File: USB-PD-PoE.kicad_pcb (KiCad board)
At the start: 4 copper layers, 39.6 x 87.4 mm, 129 parts, among them J1 8P8C_Shielded, J2 8P8C_Shielded, J3 TagConnect_TC2030_SWD, J4 USB_C_Receptacle_USB2.0, Q1 FDC2512, Q2 2N7002, Q3 2N7002, Q4 2N7002, Q5 APM4953KC, T1 HR051142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

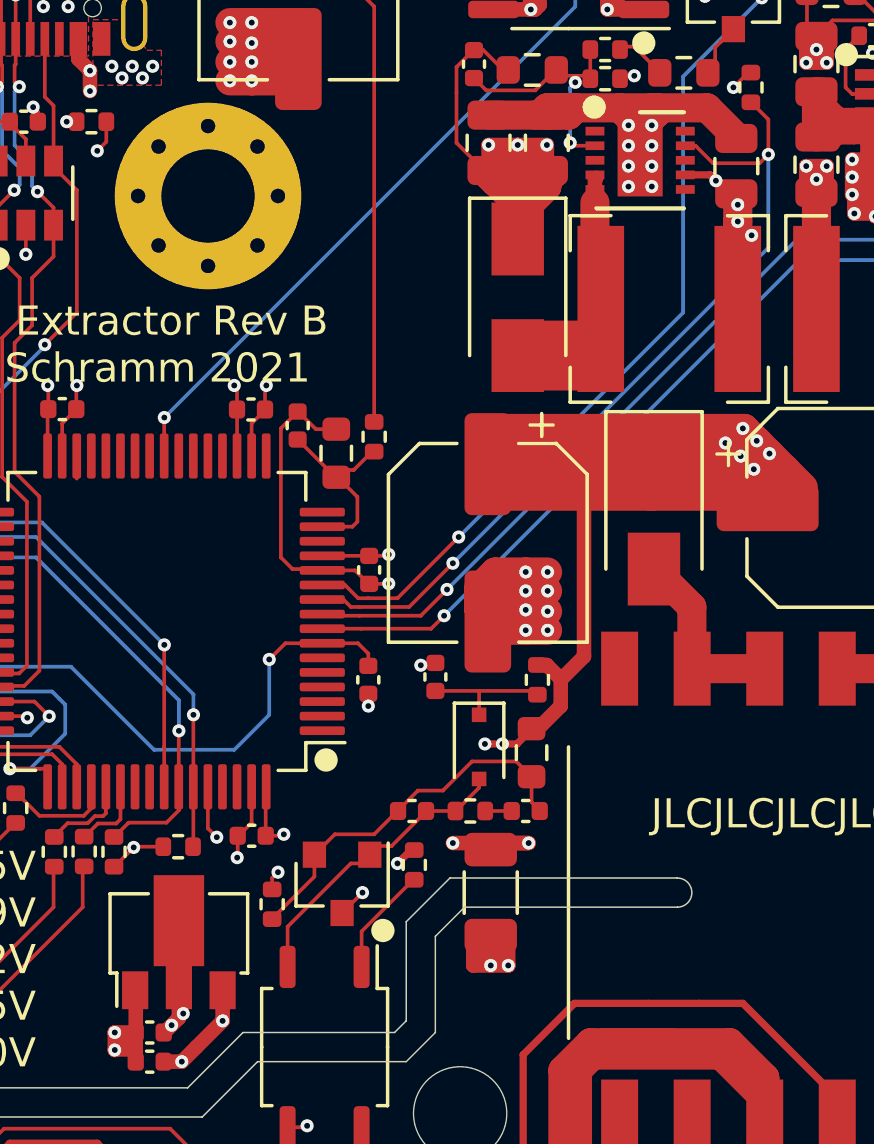
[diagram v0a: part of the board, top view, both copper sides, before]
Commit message: Fix reversed CJ431 pinout
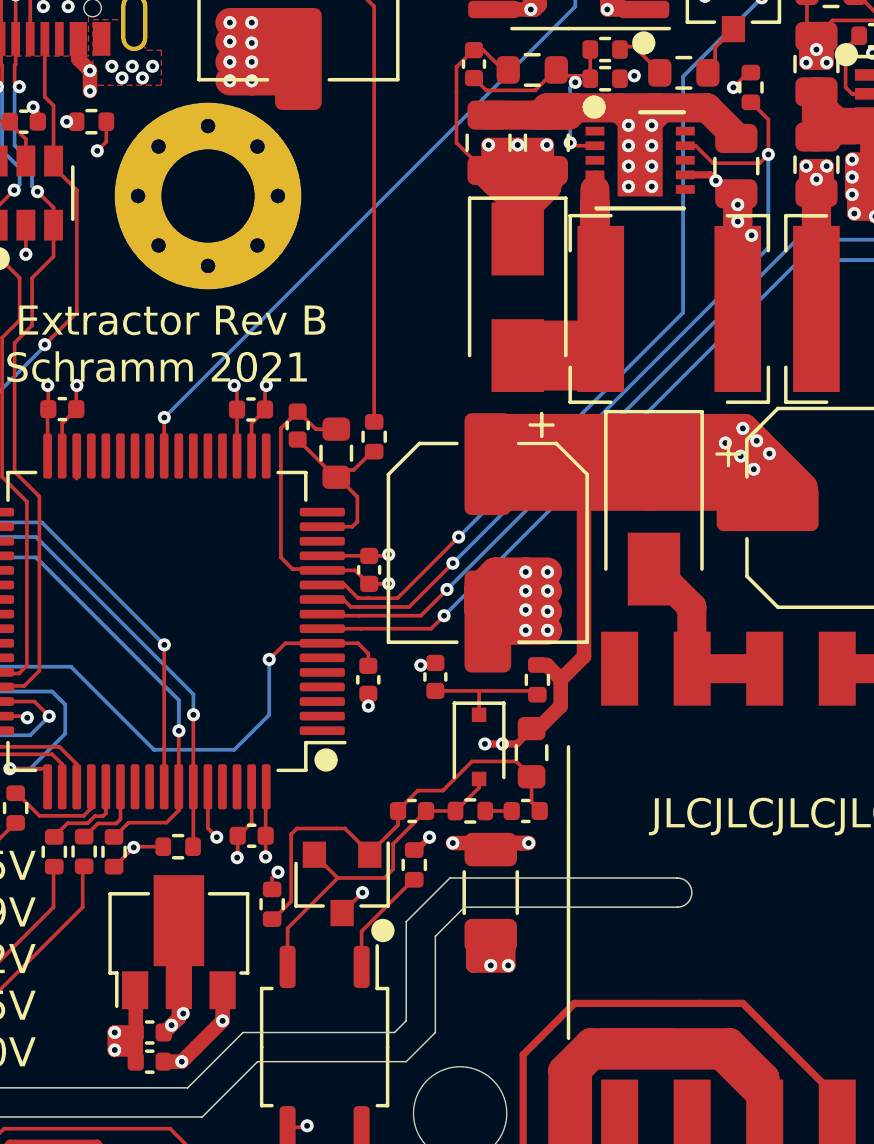
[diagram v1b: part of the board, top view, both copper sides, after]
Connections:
- U4 pad 1: Net-(C12-Pad2) -> Net-(C12-Pad1)
- U4 pad 2: Net-(C12-Pad1) -> Net-(C12-Pad2)
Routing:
- net Net-(D8-Pad2): track 19.7 -> 23.9 mm
- net Net-(C12-Pad1): track 13.1 -> 15.3 mm
- net Net-(C12-Pad2): track 9.97 -> 11.8 mm

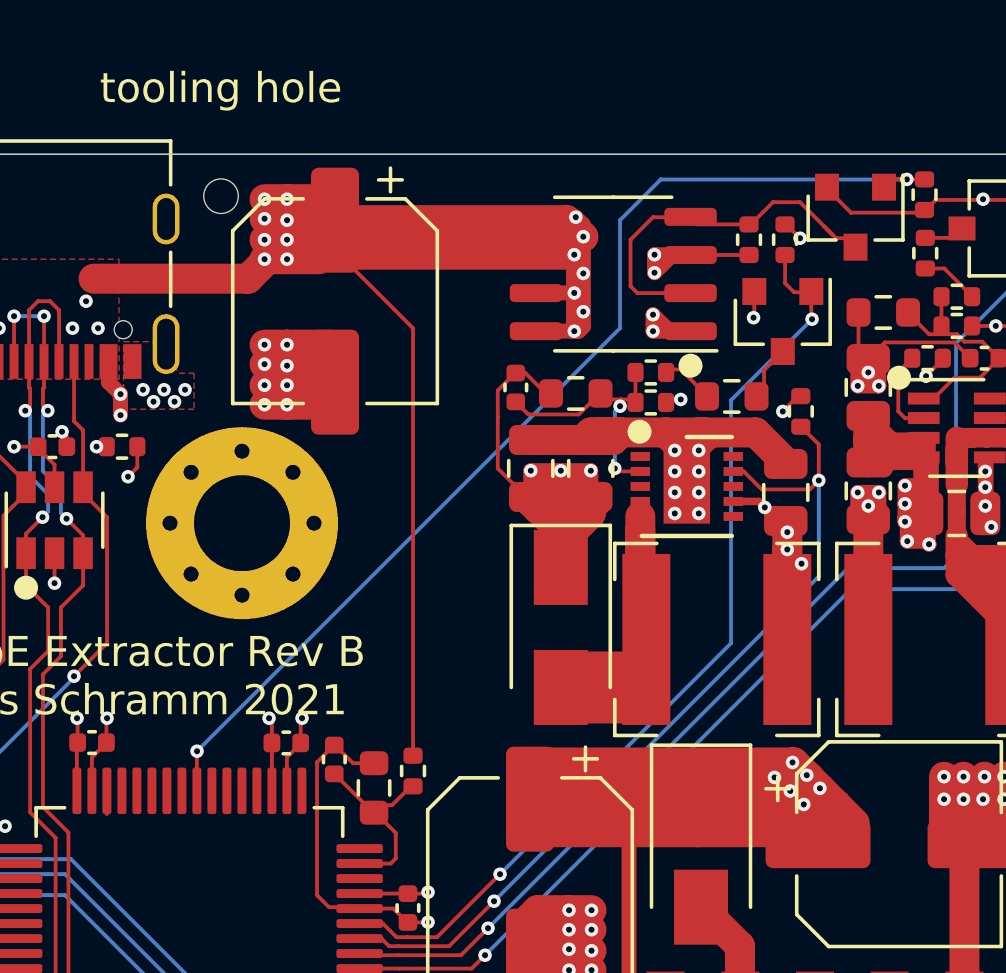
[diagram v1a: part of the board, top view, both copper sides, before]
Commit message: Add buck converter power gating
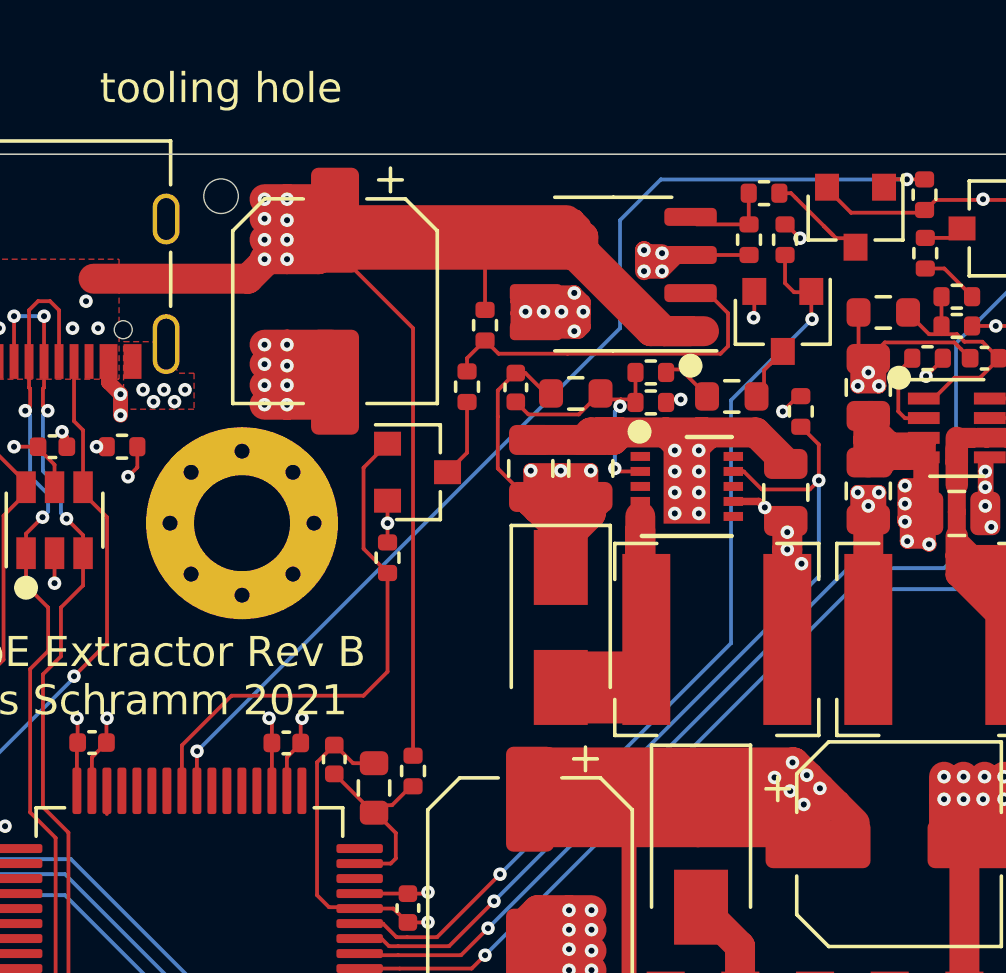
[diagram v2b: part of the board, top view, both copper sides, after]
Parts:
- added Q6: 2N7002, Package_TO_SOT_SMD:SOT-23, F.Cu at (118.5, 76.6)
- added R50: 100kR, Resistor_SMD:R_0402_1005Metric, F.Cu at (117.5, 79.5)
- added R51: 100kR, Resistor_SMD:R_0402_1005Metric, F.Cu at (120.7, 71.7)
- added R52: 15kR, Resistor_SMD:R_0402_1005Metric, F.Cu at (120.1, 73.8)
- added R53: 10kR, Resistor_SMD:R_0402_1005Metric, F.Cu at (130.0, 67.3)
- C10, C11: value 22uF EL -> 220uF EL
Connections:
- C29 pad 1: VBUS -> /BUCK_OUT
- C31 pad 1: VBUS -> /BUCK_OUT
- C39 pad 1: VBUS -> /BUCK_OUT
- L3 pad 2: VBUS -> /BUCK_OUT
- Q5 pad 1: /BOOST_OUT -> VBUS
- Q5 pad 2: Net-(Q4-Pad3) -> Net-(Q5-Pad2)
- Q5 pad 4: Net-(Q4-Pad3) -> Net-(Q5-Pad4)
- Q5 pad 7: VBUS -> /BUCK_OUT
- Q5 pad 8: VBUS -> /BUCK_OUT
- R31 pad 1: VBUS -> /BUCK_OUT
- R39 pad 1: Net-(Q4-Pad3) -> Net-(Q5-Pad4)
- U1 pad 25: Net-(U1-Pad25) -> /BUCK_OUT_EN
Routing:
- net /BUCK_OUT: track 0.00 -> 67.5 mm, vias 0 -> 12
- net VBUS: track 153.8 -> 103.2 mm, vias 32 -> 19
- net /BUCK_OUT_EN: track 0.00 -> 17.6 mm
- net Net-(Q5-Pad2): track 0.00 -> 12.3 mm
- net Net-(Q4-Pad3): track 12.6 -> 3.72 mm
- net Net-(Q5-Pad4): track 0.00 -> 2.75 mm
- net Net-(Q6-Pad3): track 0.00 -> 2.61 mm
- net GND: track 151.2 -> 152.6 mm, vias 80 -> 81
- net /BOOST_OUT: track 60.3 -> 59.4 mm

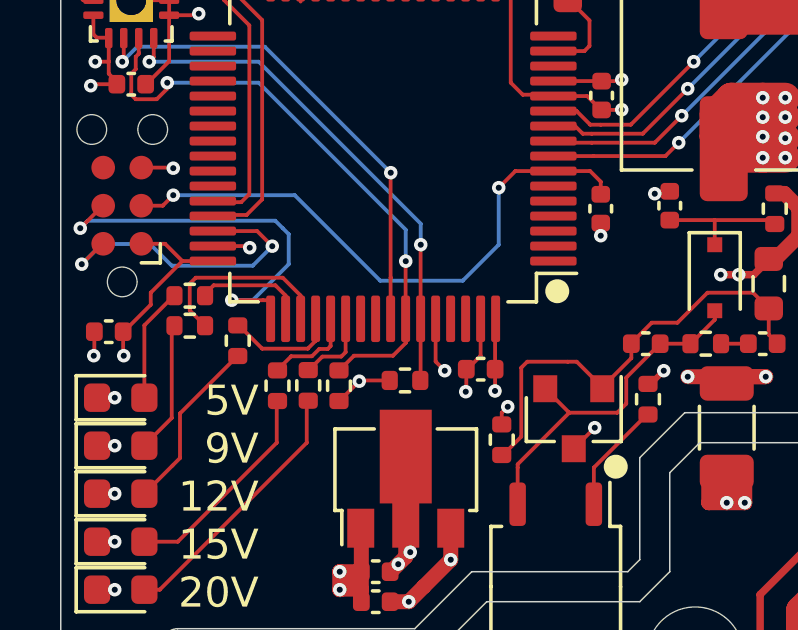
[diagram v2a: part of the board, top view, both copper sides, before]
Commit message: Move 5V LED away from JTAG pins
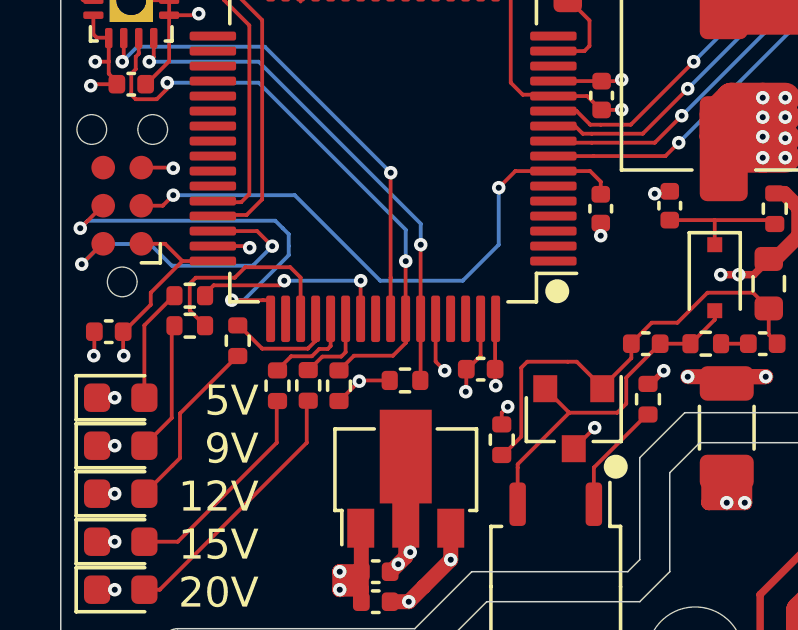
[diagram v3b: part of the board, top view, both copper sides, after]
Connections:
- U1 pad 50: /LED_5V -> Net-(U1-Pad50)
- U1 pad 55: Net-(U1-Pad55) -> /LED_5V
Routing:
- net /LED_5V: track 3.73 -> 6.66 mm, vias 0 -> 2
- net /SWCLK: track 14.0 -> 13.2 mm
- net /LED_9V: track 6.41 -> 7.05 mm

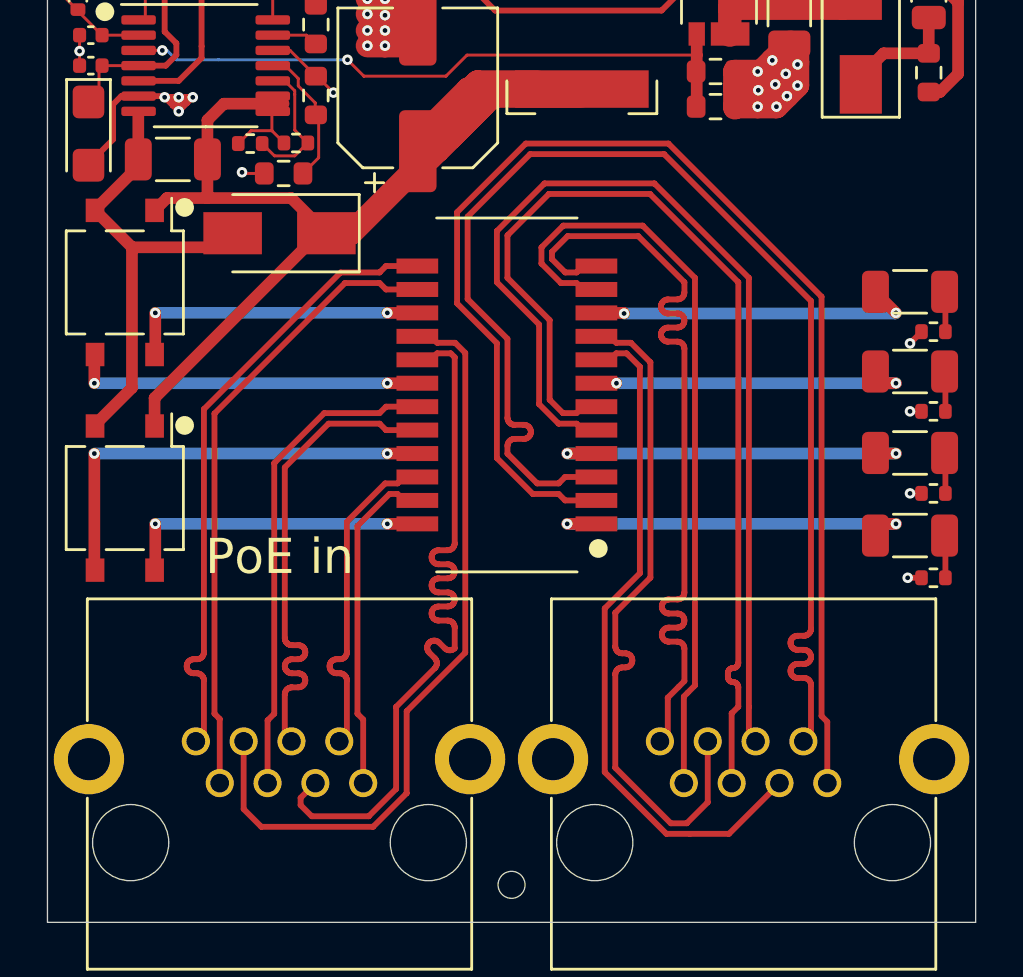
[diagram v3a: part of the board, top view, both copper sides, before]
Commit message: Fix ethernet transformer footprint
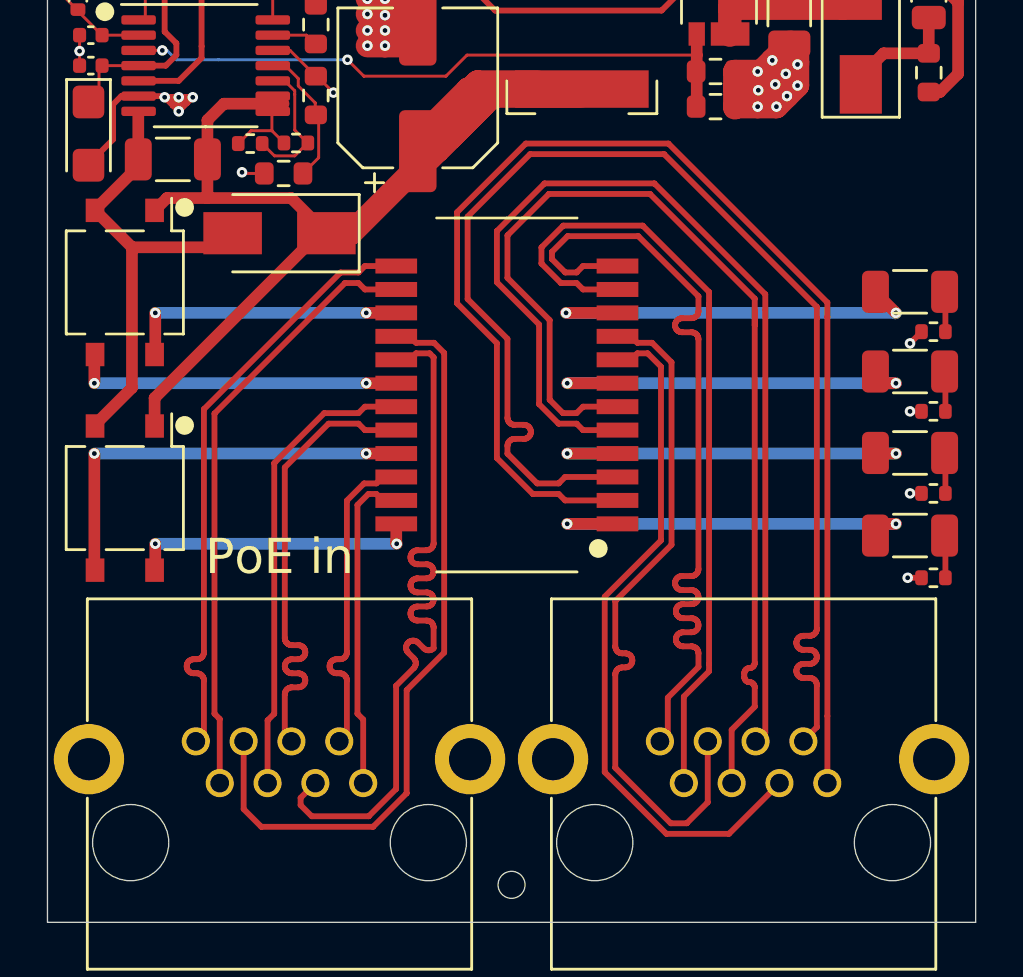
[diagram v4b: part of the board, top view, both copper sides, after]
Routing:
- net Net-(C20-Pad2): track 14.1 -> 17.6 mm
- net Net-(C19-Pad2): track 13.7 -> 17.1 mm
- net /ETH_DEV3+: track 44.2 -> 46.4 mm
- net /ETH_DEV3-: track 44.1 -> 45.9 mm
- net /ETH_DEV4+: track 56.5 -> 58.1 mm
- net /ETH_DEV1-: track 33.1 -> 34.5 mm
- net /ETH_DEV1+: track 35.1 -> 36.5 mm
- net Net-(C18-Pad2): track 16.2 -> 17.1 mm
- net Net-(C17-Pad2): track 16.2 -> 17.1 mm
- net Net-(D2-Pad4): track 12.9 -> 12.0 mm
- net Net-(D2-Pad3): track 15.0 -> 14.1 mm
- net Net-(D1-Pad3): track 18.8 -> 17.9 mm
- net /ETH_POE1+: track 26.9 -> 26.0 mm
- net /ETH_POE3-: track 20.9 -> 20.0 mm
- net /ETH_POE3+: track 20.9 -> 20.0 mm
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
